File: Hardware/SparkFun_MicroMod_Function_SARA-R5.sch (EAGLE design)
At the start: 93 parts, among them IC2 SN74AVC4T774PW, J1 MICROMOD_FUNCTION_STANDARD, J2 U.FL, J4 U.FL, J9 NANO_SIM, Q2 310mA/60V/1.6Ω, Q3 310mA/60V/1.6Ω, Q5 310mA/60V/1.6Ω, Q6 310mA/60V/1.6Ω, U1 SARA-R510M8S, U11 74HC1G04, U3 3.3V, U4 EEPROM, U8 AP7361C-33FGE

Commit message: pre-review changes (part 1)
-renamed all jumpers to match silk
-replaced I2C pullups to 2.2K
-Schematic Cleanup
-silk lines between tight passives in a row
-fixed acid trap off of pad 12
-tweaked via position near GND pad 14 to allow for flow
-routed GND to connect inner and perimeter GND pads on module.
-nudging of vias and traces to improve some gnd pour flow
-added mini VCC polygon over m.2 connector pads for better flow
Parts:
- R10, R6: value 4.7k -> 2.2k; device SparkFun-Resistors:4.7KOHM-0402T-1/16W-1% -> SparkFun-Resistors:2.2KOHM-0402T-1/16W-1%
- renumbered JP1 to 3V3_LED, JP2 to I2C, JP3 to WP, JP4 to ANT_REG_EN, JP5 to LTE_PWR_ON, JP6 to LTE_NI, JP7 to LTE_ON, JP8 to LTE_RESET
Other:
- note added: "Cut jumper to disable D3 power LED"
- note removed: "Cut JP1 to disable D3 power LED"
- moved on the sheet: C1, C18, C19, C2, C20, C22, C24, C3, C33, C36, C37, C38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

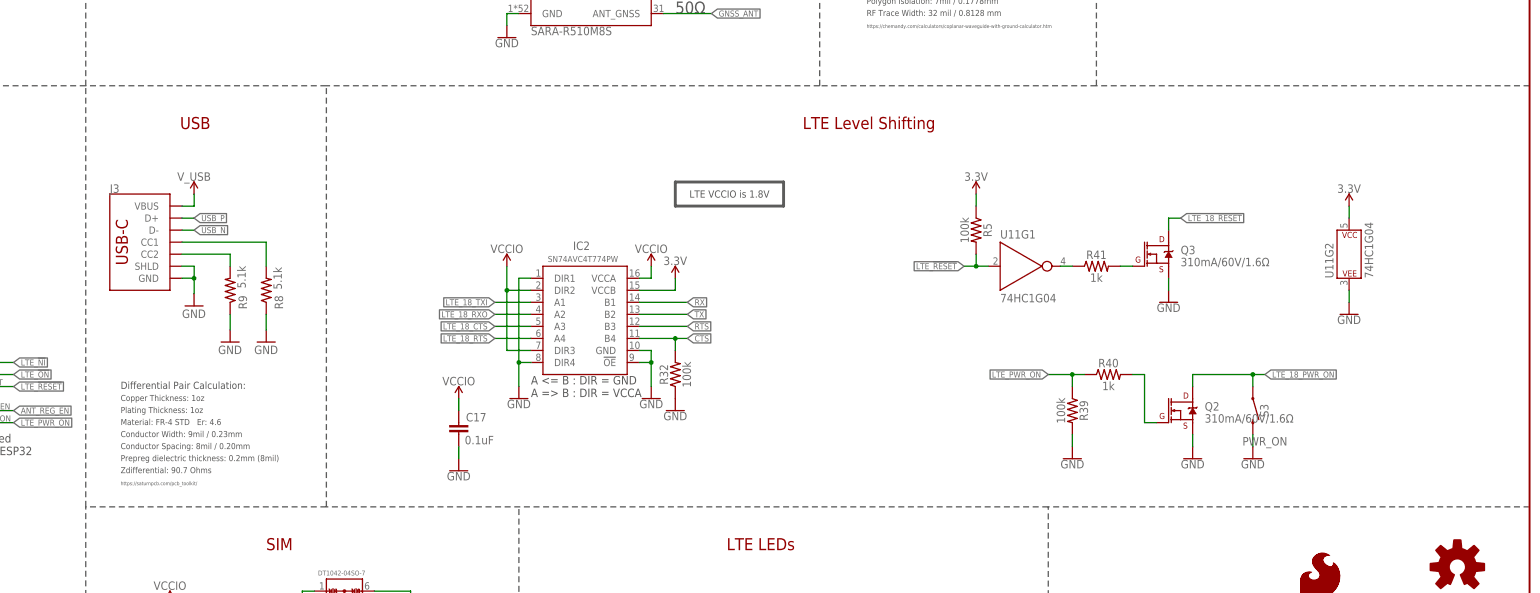
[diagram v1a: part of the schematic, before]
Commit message: USB_SHLD jumper added
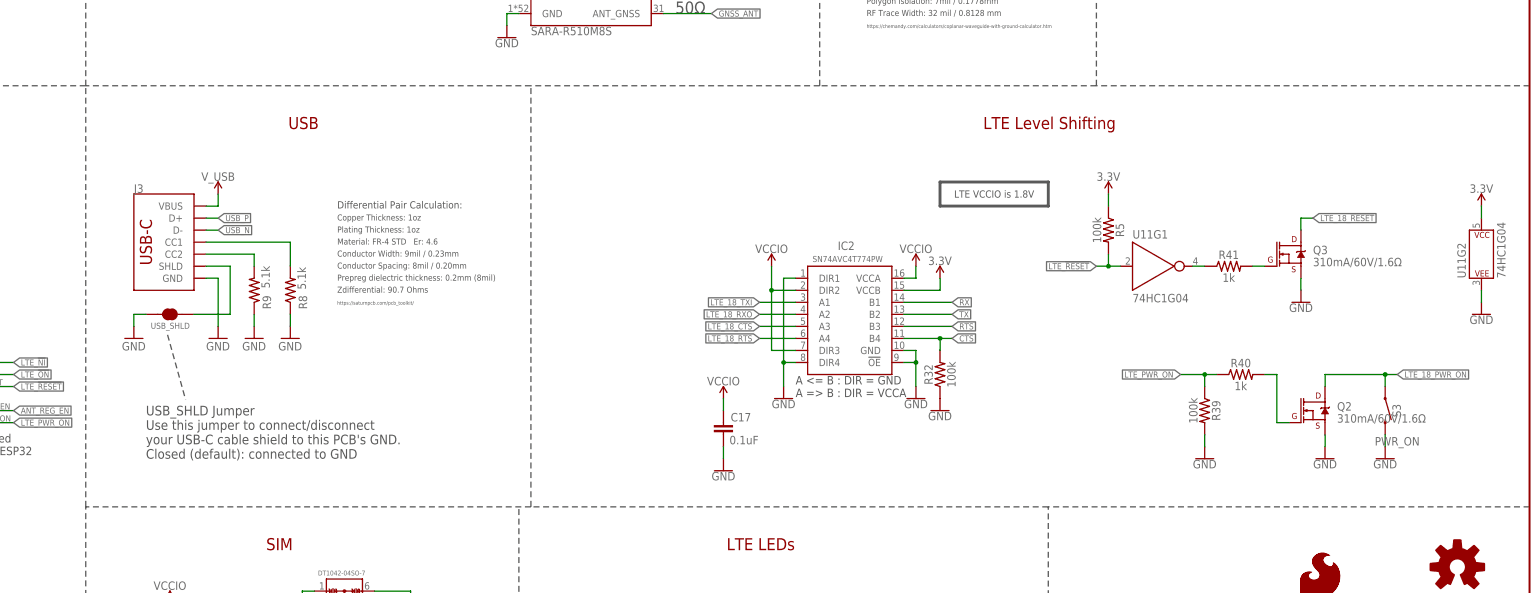
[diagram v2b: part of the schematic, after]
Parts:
- added USB_SHLD: JUMPER-SMT_2_NC_TRACE_SILK, SparkFun-Jumpers:JUMPER-SMT_2_NC_TRACE_SILK
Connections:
- new net SHLD: J3.SHLD, USB_SHLD.1
- net GND: now also USB_SHLD.2; no longer J3.SHLD
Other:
- note added: "USB_SHLD Jumper Use this jumper to connect/disconnect your USB-C cable shield to this PCB's GND. Closed (default): connected to GND"
- moved on the sheet: C17, IC2, J3, Q2, Q3, R32, R39, R40, R41, R5, R8, R9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

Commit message: Sim connector re-routing
-IC2 ref to U2
-Updated Nano SIM FP to have tRestrict area underneath
-moved traces under the SIM connector to bottom layer
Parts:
- renumbered IC2 to U2, U8 to U5
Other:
- moved on the sheet: Q2, R39, R40, S3

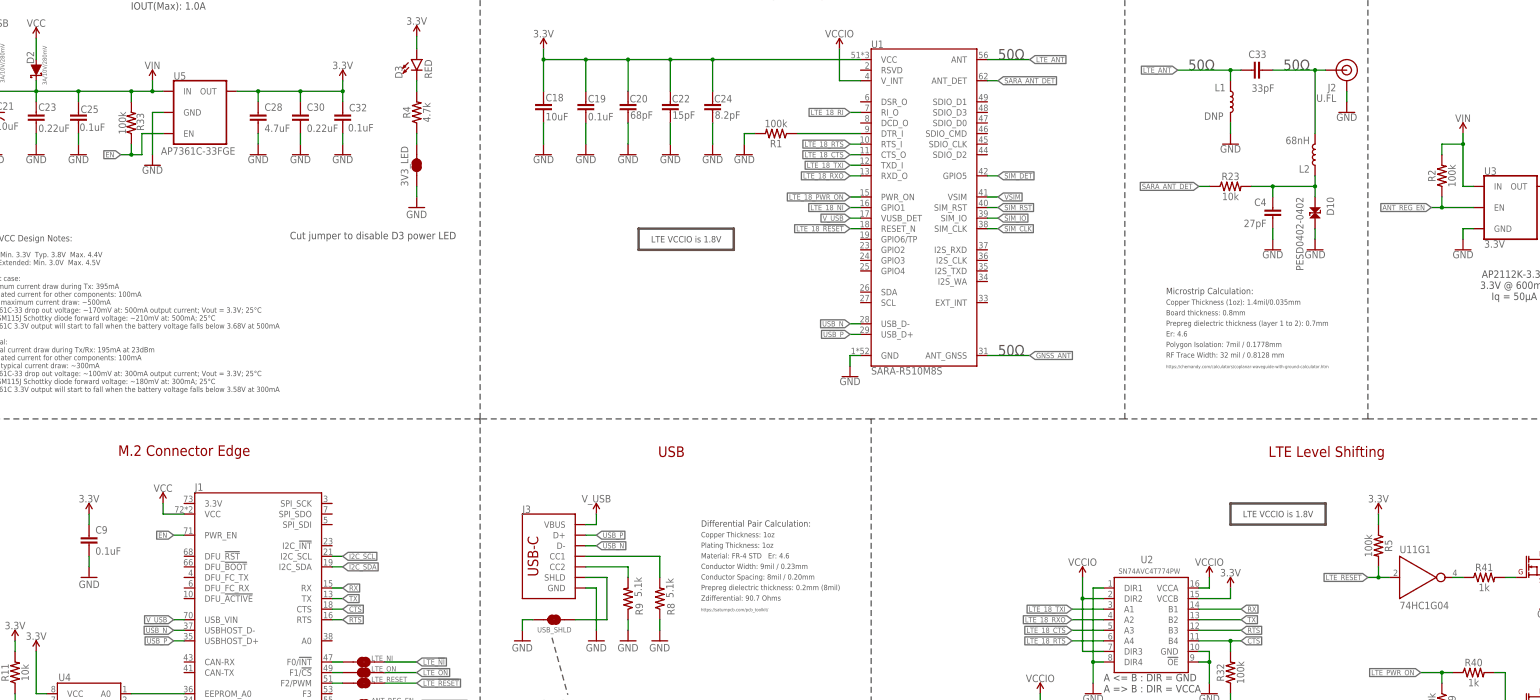
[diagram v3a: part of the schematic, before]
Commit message: More changes from group review
-Now it's a 4-layer, removed some 3.3V traces from bottom copper, added vias as necessary to connect to 3.3V inner layer.
-Changed where regulators (U3 and U5) enable pins are tied up to. They are now tied up to the 3.3V provided by the MM Main board. Previously, they were connected to VIN, which could be higher than 3.3V and damage enable control GPIO on some processor boards.
-Disconnected V_USB from MM m.2 connector.
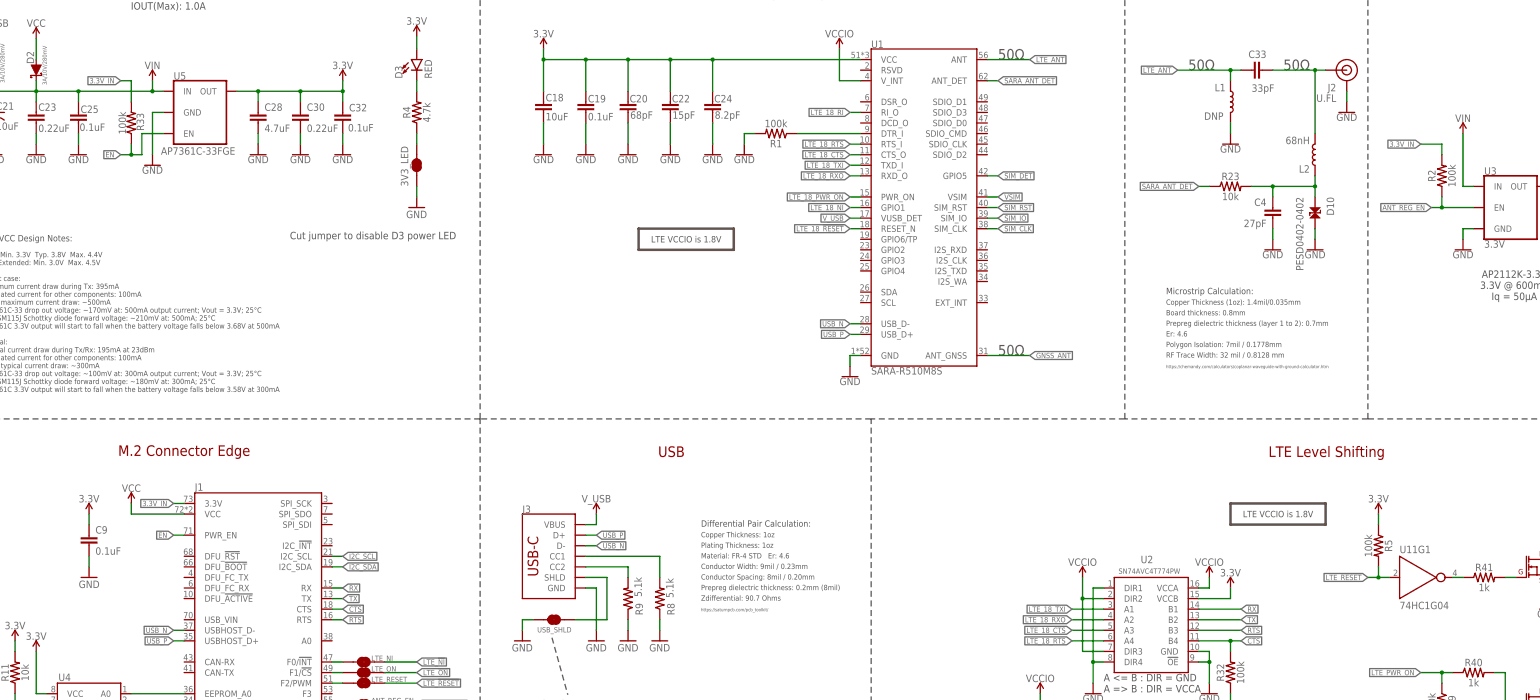
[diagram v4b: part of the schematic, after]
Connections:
- new net 3.3V_IN: J1.3.3V, R2.2, R33.2
- net VIN: no longer R2.2, R33.2
- net V_USB: no longer J1.USB_VIN
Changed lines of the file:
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@@
 <attribute name="VALUE" x="20.32" y="261.874" size="1.778" layer="96" font="vector" align="bottom-center"/>
 </instance>
-<instance part="SUPPLY1" gate="G$1" x="50.8" y="147.32" smashed="yes">
-<attribute name="VALUE" x="50.8" y="150.114" size="1.778" layer="96" font="vector" align="bottom-center"/>
+<instance part="SUPPLY1" gate="G$1" x="43.18" y="147.32" smashed="yes">
+<attribute name="VALUE" x="43.18" y="150.114" size="1.778" layer="96" font="vector" align="bottom-center"/>
 </instance>
 <instance part="GND4" gate="1" x="45.72" y="83.82" smashed="yes">
@@
 <pinref part="J1" gate="J1" pin="VCC"/>
 <pinref part="SUPPLY1" gate="G$1" pin="VCC"/>
-<wire x1="55.88" y1="144.78" x2="50.8" y2="144.78" width="0.1524" layer="91"/>
-<wire x1="50.8" y1="144.78" x2="50.8" y2="147.32" width="0.1524" layer="91"/>
+<wire x1="55.88" y1="144.78" x2="43.18" y2="144.78" width="0.1524" layer="91"/>
+<wire x1="43.18" y1="144.78" x2="43.18" y2="147.32" width="0.1524" layer="91"/>
 </segment>
 <segment>
@@
 <label x="215.9" y="215.9" size="1.27" layer="95" font="vector" rot="R180" xref="yes"/>
 <pinref part="U1" gate="G$2" pin="VUSB_DET"/>
-</segment>
-<segment>
-<pinref part="J1" gate="J1" pin="USB_VIN"/>
-<wire x1="55.88" y1="119.38" x2="53.34" y2="119.38" width="0.1524" layer="91"/>
-<label x="53.34" y="119.38" size="1.27" layer="95" font="vector" rot="R180" xref="yes"/>
 </segment>
 </net>
@@
 <wire x1="365.76" y1="223.52" x2="363.22" y2="223.52" width="0.1524" layer="91"/>
 <pinref part="SUPPLY3" gate="G$1" pin="VIN"/>
-<wire x1="363.22" y1="223.52" x2="363.22" y2="233.68" width="0.1524" layer="91"/>
-<pinref part="R2" gate="G$1" pin="2"/>
-<wire x1="363.22" y1="233.68" x2="363.22" y2="236.22" width="0.1524" layer="91"/>
-<wire x1="358.14" y1="231.14" x2="358.14" y2="233.68" width="0.1524" layer="91"/>
-<wire x1="358.14" y1="233.68" x2="363.22" y2="233.68" width="0.1524" layer="91"/>
-<junction x="363.22" y="233.68"/>
+<wire x1="363.22" y1="223.52" x2="363.22" y2="236.22" width="0.1524" layer="91"/>
 </segment>
 <segment>
@@
 <wire x1="50.8" y1="246.38" x2="48.26" y2="246.38" width="0.1524" layer="91"/>
 <pinref part="C23" gate="G$1" pin="1"/>
-<wire x1="48.26" y1="246.38" x2="43.18" y2="246.38" width="0.1524" layer="91"/>
-<wire x1="43.18" y1="243.84" x2="43.18" y2="246.38" width="0.1524" layer="91"/>
-<wire x1="43.18" y1="246.38" x2="30.48" y2="246.38" width="0.1524" layer="91"/>
+<wire x1="48.26" y1="246.38" x2="30.48" y2="246.38" width="0.1524" layer="91"/>
 <wire x1="30.48" y1="246.38" x2="20.32" y2="246.38" width="0.1524" layer="91"/>
 <wire x1="20.32" y1="246.38" x2="20.32" y2="243.84" width="0.1524" layer="91"/>
@@
 <wire x1="30.48" y1="243.84" x2="30.48" y2="246.38" width="0.1524" layer="91"/>
 <junction x="30.48" y="246.38"/>
-<pinref part="R33" gate="G$1" pin="2"/>
 <pinref part="D1" gate="G$1" pin="C"/>
 <wire x1="10.16" y1="248.92" x2="10.16" y2="246.38" width="0.1524" layer="91"/>
@@
 <wire x1="48.26" y1="248.92" x2="48.26" y2="246.38" width="0.1524" layer="91"/>
 <junction x="48.26" y="246.38"/>
-<junction x="43.18" y="246.38"/>
 </segment>
 </net>
@@
 </segment>
 </net>
+<net name="3.3V_IN" class="0">
+<segment>
+<pinref part="J1" gate="J1" pin="3.3V"/>
+<wire x1="55.88" y1="147.32" x2="53.34" y2="147.32" width="0.1524" layer="91"/>
+<label x="53.34" y="147.32" size="1.27" layer="95" font="vector" rot="R180" xref="yes"/>
+</segment>
+<segment>
+<wire x1="43.18" y1="248.92" x2="40.64" y2="248.92" width="0.1524" layer="91"/>
+<label x="40.64" y="248.92" size="1.27" layer="95" font="vector" rot="R180" xref="yes"/>
+<pinref part="R33" gate="G$1" pin="2"/>
+<wire x1="43.18" y1="243.84" x2="43.18" y2="248.92" width="0.1524" layer="91"/>
+</segment>
+<segment>
+<label x="353.06" y="233.68" size="1.27" layer="95" font="vector" rot="R180" xref="yes"/>
+<pinref part="R2" gate="G$1" pin="2"/>
+<wire x1="358.14" y1="231.14" x2="358.14" y2="233.68" width="0.1524" layer="91"/>
+<wire x1="358.14" y1="233.68" x2="353.06" y2="233.68" width="0.1524" layer="91"/>
+</segment>
+</net>

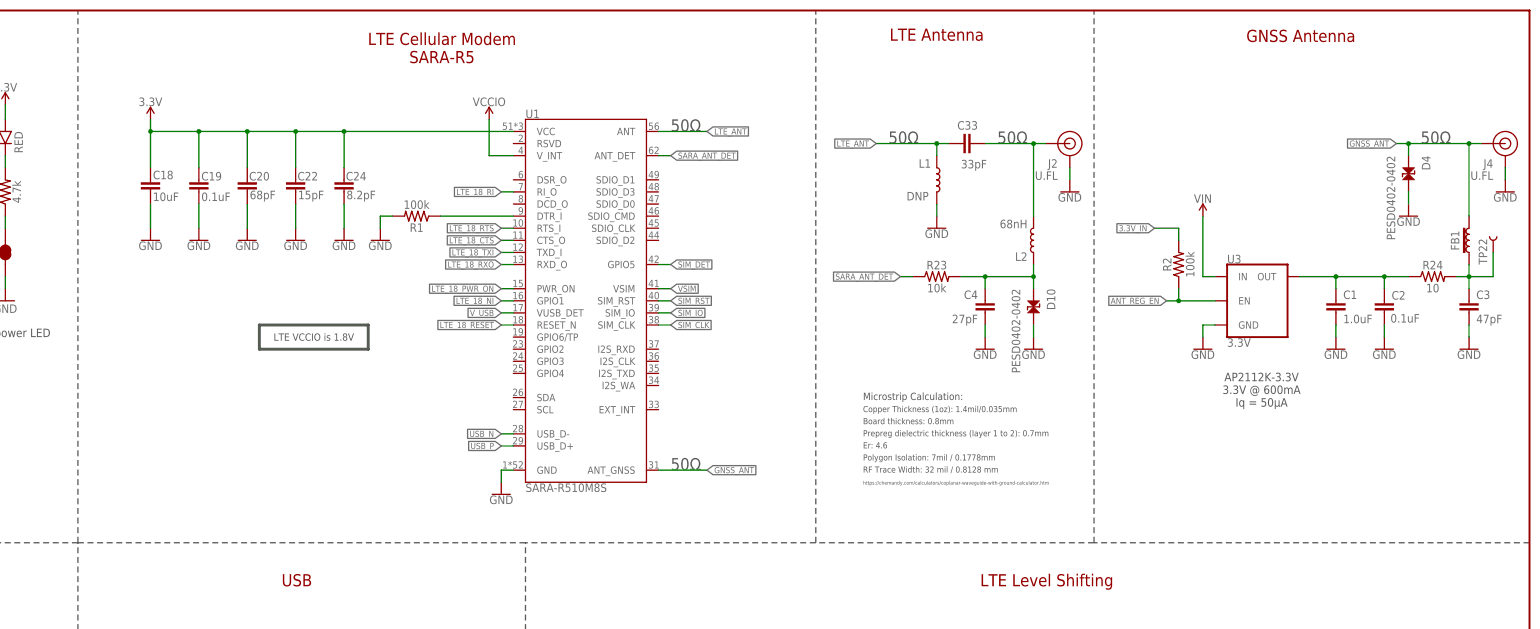
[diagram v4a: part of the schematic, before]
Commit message: ESD diode position and removed L1
-Moved ESD diode D10 to the other side of L2, to put it directly next to the u.fl connector
-removed L1 (it was previously DNP)
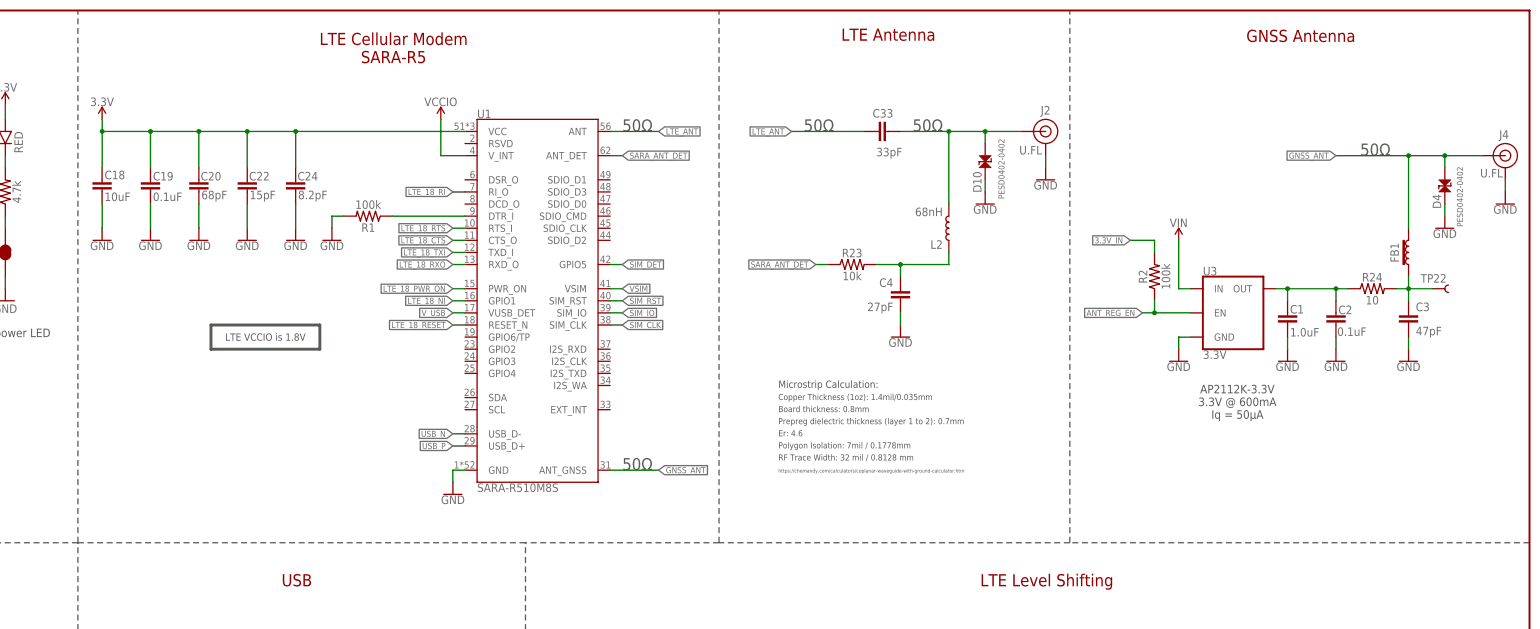
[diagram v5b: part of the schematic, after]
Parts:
- removed L1: DNP, New_Parts:INDUCTOR_DNP-0402
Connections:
- net GND: no longer L1.2
- net LTE_ANT: no longer L1.1
- net N$11: now also D10.1
- net N$18: no longer D10.1
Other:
- moved on the sheet: C1, C18, C19, C2, C20, C22, C24, C3, C33, C4, D10, D4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

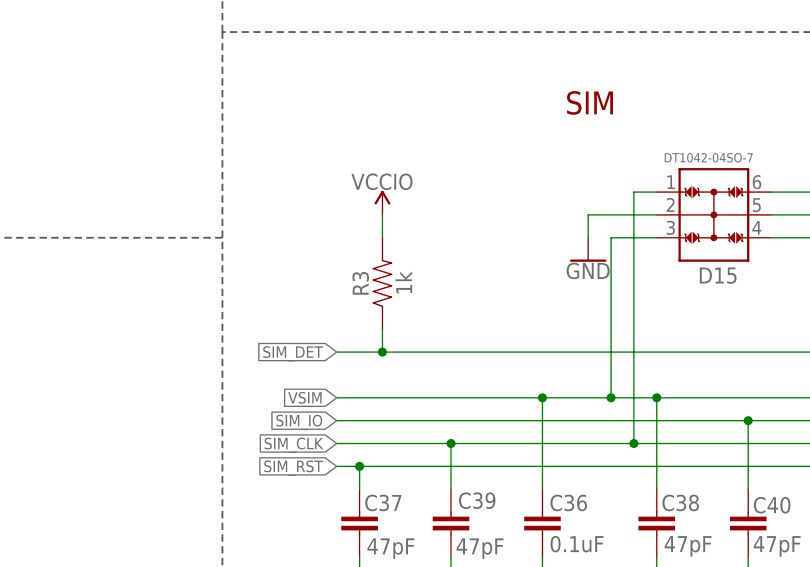
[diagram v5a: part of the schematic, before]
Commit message: acid traps and measures
-fixed some acid traps and routed some GNDs off of pads
-measures to everything
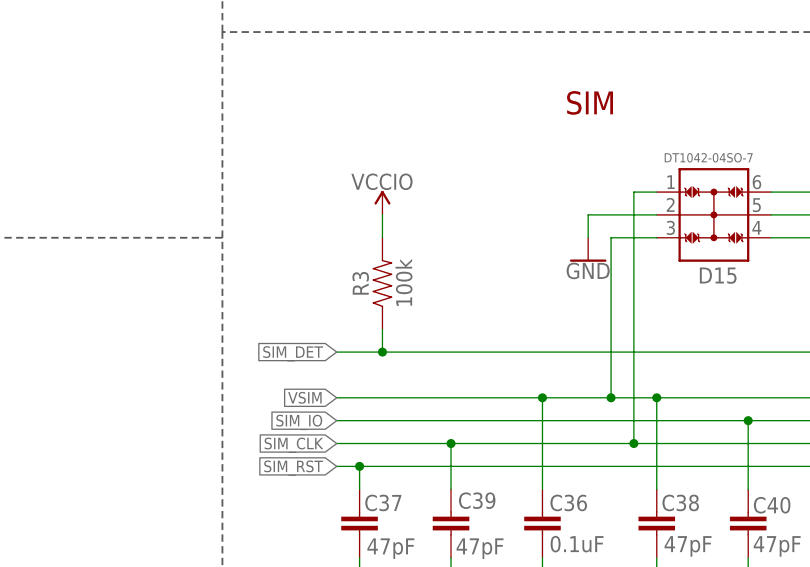
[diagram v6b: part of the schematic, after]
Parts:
- R3: value 1k -> 100k; device SparkFun-Resistors:1KOHM-0402T-1/16W-1% -> SparkFun-Resistors:100KOHM-0402T-1/16W-1%
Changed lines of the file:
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@@
 <part name="J2" library="SparkFun-Connectors" deviceset="U.FL2PIN" device="" value="U.FL"/>
 <part name="J9" library="HPG_Solution_v1.0" deviceset="SIMHOLDER" device="-PUSHPUSH" value="NANO_SIM"/>
-<part name="R3" library="SparkFun-Resistors" deviceset="1KOHM" device="-0402T-1/16W-1%" value="1k"/>
+<part name="R3" library="SparkFun-Resistors" deviceset="100KOHM" device="-0402T-1/16W-1%" value="100k"/>
 <part name="SUPPLY13" library="SparkFun-PowerSymbols" deviceset="VCCIO" device=""/>
 <part name="LOGO1" library="SparkFun-Aesthetics" deviceset="SFE_LOGO_NAME_FLAME" device=".2_INCH"/>
